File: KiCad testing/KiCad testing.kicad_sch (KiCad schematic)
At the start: 41 parts, among them J1 USB_A, Q1 IRF540N, Q2 IRF540N, Q3 IRF540N, U1 IR2113S, U2 IR2113S, U3 ACS712xLCTR-05B

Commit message: Update Schematic
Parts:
- removed U1, U2: IR2113S, Package_DIP:DIP-14_W7.62mm_Socket, symbol Driver_FET:IR2113S
- added U1, U4: IR2213, Package_DIP:DIP-14_W7.62mm, symbol Driver_FET:IR2213
- C1: renamed from C6; footprint (none) -> Capacitor_THT:CP_Radial_D5.0mm_P2.00mm
- C2: renamed from C9; footprint (none) -> Capacitor_THT:CP_Radial_D5.0mm_P2.00mm
- C3: footprint (none) -> Capacitor_THT:CP_Radial_D6.3mm_P2.50mm
- C4, C8: footprint (none) -> Capacitor_THT:C_Disc_D4.7mm_W2.5mm_P5.00mm
- C5: renamed from C7; footprint (none) -> Capacitor_THT:CP_Radial_D5.0mm_P2.00mm
- C6: renamed from C10; footprint (none) -> Capacitor_THT:CP_Radial_D5.0mm_P2.00mm
- C7: renamed from C11; footprint (none) -> Capacitor_THT:CP_Radial_D6.3mm_P2.50mm
- renumbered C12 to C10, C1 to C11, C5 to C12, C2 to C9, D2 to D1, D3 to D2, D5 to D3, D1 to D5, R5 to R2, R2 to R4, R6 to R5, R4 to R6, R9 to Rb1, R11 to Rb2
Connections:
- net +Buck_Boost_Load: now also U1.11 (SD), U1.13 (VSS), U1.2 (COM), U4.11 (SD), U4.13 (VSS), U4.2 (COM)
- net 12V: now also U1.3 (VCC), U4.3 (VCC)
- net 5V: now also U1.9 (VDD), U4.9 (VDD)
- net PWM_High: now also U4.10 (HIN)
- net PWM_Low: now also U4.12 (LIN)
- net PWM_MPPT: now also U1.10 (HIN)
- net VS: now also U4.5 (VS); no longer C6.2, R5.1
- net at R1.2: now also U4.1 (LO)
- net at C2.1, C3.1, C4.2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: now also U4.6 (VB)
- net at R3.1: now also U4.7 (HO)
- net at R4.2: now also U1.1 (LO)
- net at C6.1, C7.1, C8.2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: now also U1.6 (VB)
- net at R6.1: now also U1.7 (HO)
- new net VS_1: C6.2, R5.1, U1.5 (VS)

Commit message: Update Schematic
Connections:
- net PWM_High: now also A1.13 (D10); no longer A1.12 (D9)
- net PWM_Low: now also A1.12 (D9); no longer A1.13 (D10)

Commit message: Update Schematic
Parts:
- C2, C6: value 10uF -> 470uF; footprint Capacitor_THT:CP_Radial_D5.0mm_P2.00mm -> Capacitor_THT:CP_Radial_D10.0mm_P5.00mm
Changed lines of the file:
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@@
       (effects (font (size 1.27 1.27)) (justify right))
     )
-    (property "Value" "10uF" (at 114.173 93.599 0)
+    (property "Value" "470uF" (at 114.173 93.599 0)
       (effects (font (size 1.27 1.27)) (justify right))
     )
-    (property "Footprint" "Capacitor_THT:CP_Radial_D5.0mm_P2.00mm" (at 113.03 96.52 0)
+    (property "Footprint" "Capacitor_THT:CP_Radial_D10.0mm_P5.00mm" (at 113.03 96.52 0)
       (effects (font (size 1.27 1.27)) hide)
     )
@@
       (effects (font (size 1.27 1.27)) (justify right))
     )
-    (property "Value" "10uF" (at 114.173 38.989 0)
+    (property "Value" "470uF" (at 114.173 38.989 0)
       (effects (font (size 1.27 1.27)) (justify right))
     )
-    (property "Footprint" "Capacitor_THT:CP_Radial_D5.0mm_P2.00mm" (at 113.03 41.91 0)
-      (effects (font (size 1.27 1.27)) hide)
-    )
+    (property "Footprint" "Capacitor_THT:CP_Radial_D10.0mm_P5.00mm" (at 113.03 41.91 0)
+      (effects (font (size 1.27 1.27)) hide)
+    )

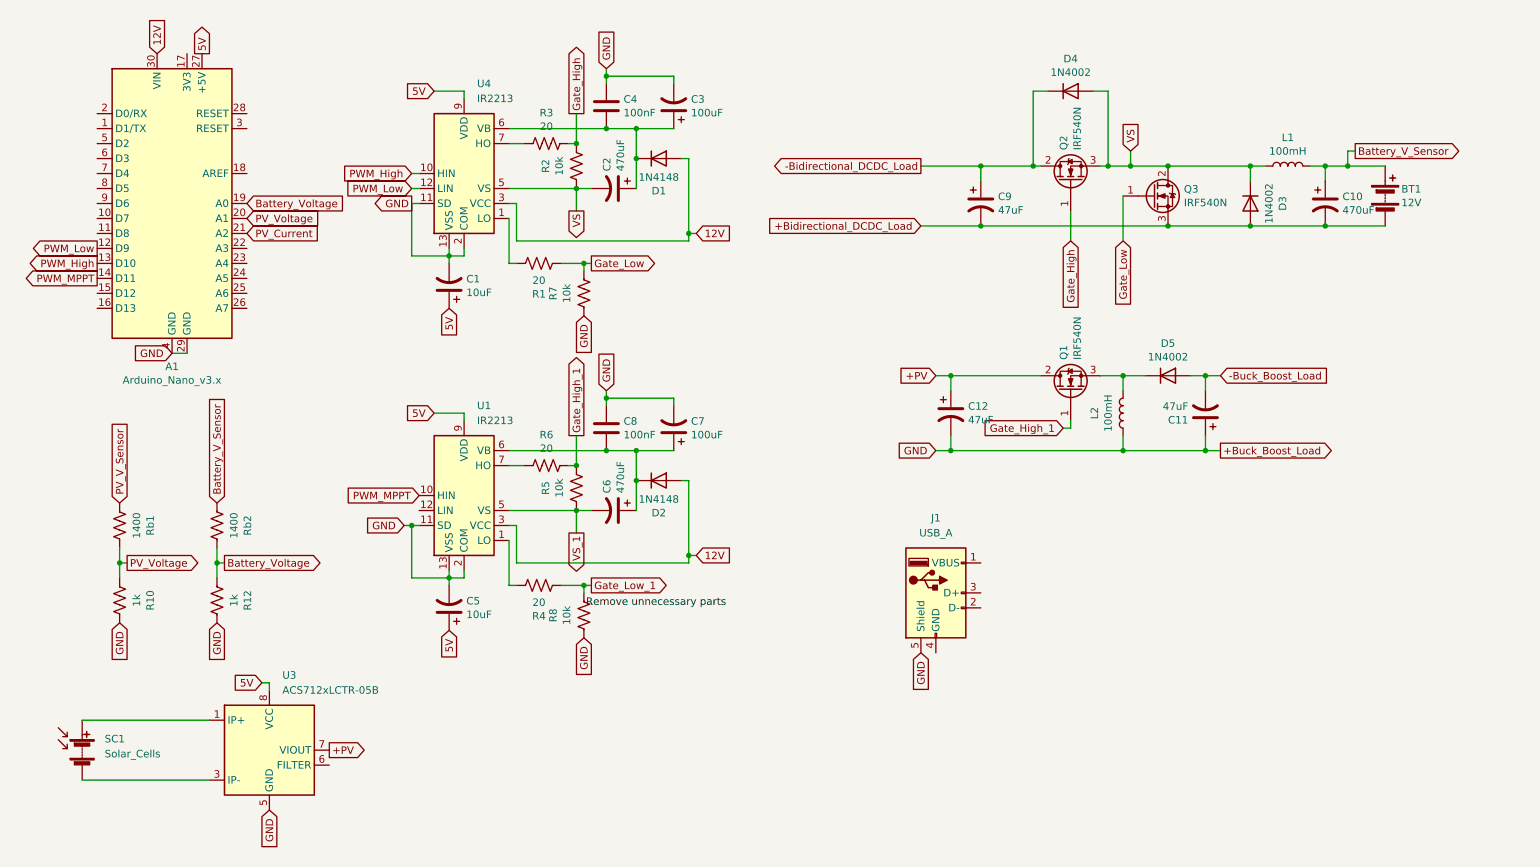
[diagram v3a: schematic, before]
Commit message: Update schematic and redesign pcb layout.
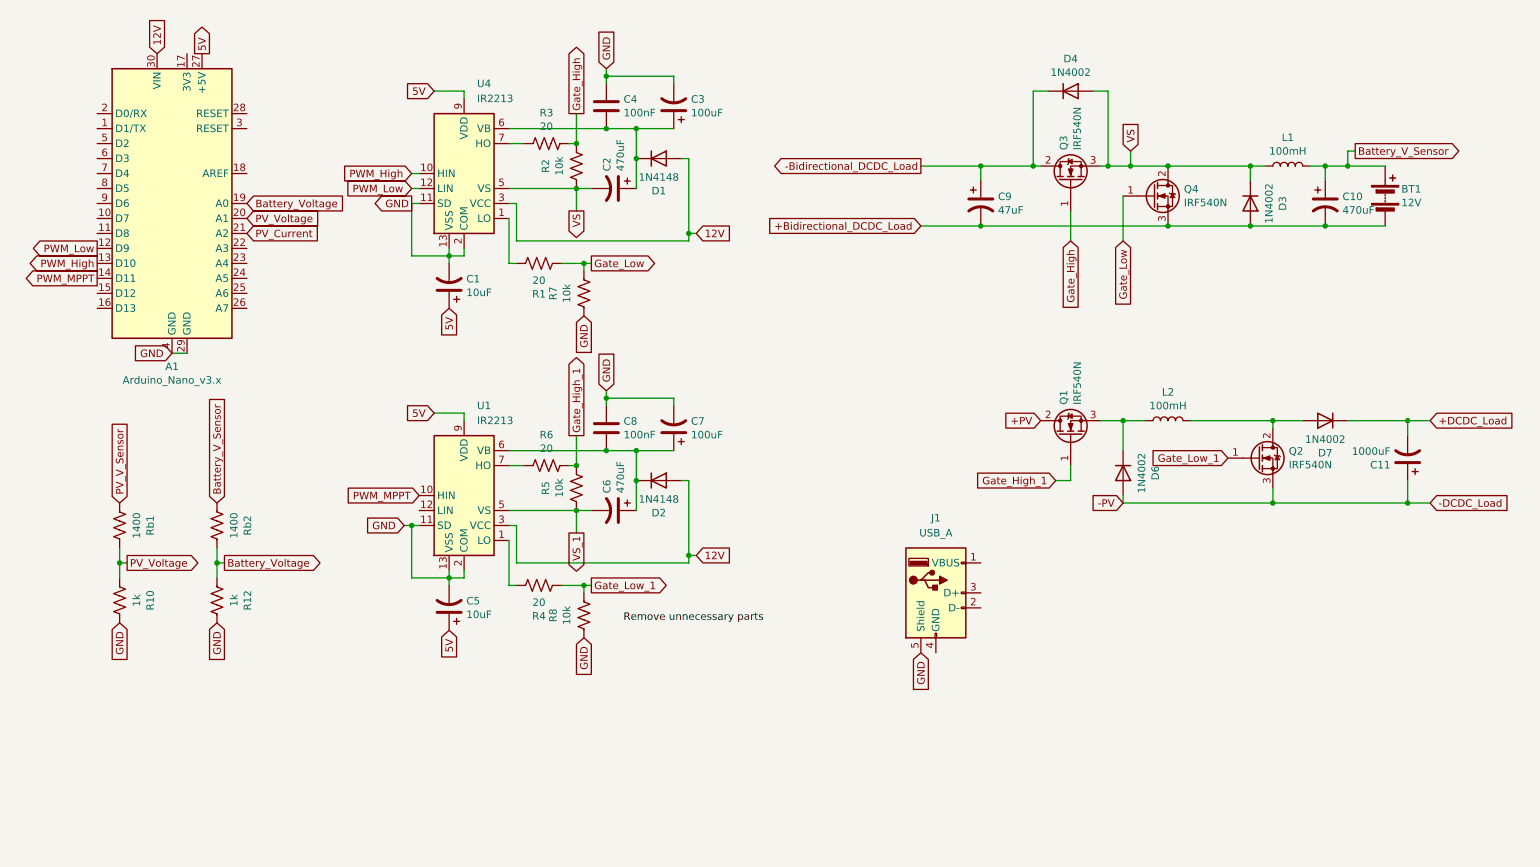
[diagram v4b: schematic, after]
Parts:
- removed C12: 47uF, Capacitor_THT:CP_Radial_D6.3mm_P2.50mm, symbol KiCad testing-rescue:CP1-Device
- removed D5: 1N4002, Diode_THT:D_DO-41_SOD81_P10.16mm_Horizontal, symbol Diode:1N4002
- removed SC1: Solar_Cells, symbol Device:Solar_Cells
- removed U3: ACS712xLCTR-05B, Package_SO:SOIC-8_3.9x4.9mm_P1.27mm, symbol Sensor_Current:ACS712xLCTR-05B
- added D6, D7: 1N4002, Diode_THT:D_DO-41_SOD81_P10.16mm_Horizontal, symbol Diode:1N4002
- added Q2: IRF540N, Package_TO_SOT_THT:TO-220-3_Vertical, symbol Transistor_FET:IRF540N
- C11: value 47uF -> 1000uF; footprint Capacitor_THT:CP_Radial_D6.3mm_P2.50mm -> Capacitor_THT:CP_Radial_D10.0mm_P5.00mm
- C3, C7: footprint Capacitor_THT:CP_Radial_D6.3mm_P2.50mm -> Capacitor_THT:CP_Radial_D5.0mm_P2.00mm
- renumbered Q2 to Q3, Q3 to Q4
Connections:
- net Gate_Low_1: now also Q2.1 (G)
- net at Q1.3 (S): now also L2.1, D6.1 (K); no longer L2.2
- net +Buck_Boost_Load renamed GND
- net GND: no longer C11.1, L2.1
- net -Buck_Boost_Load renamed +DCDC_Load
- net +DCDC_Load: now also D7.1 (K)
- new net: D7.2 (A), L2.2, Q2.2 (D)
- new net -DCDC_Load: C11.1, D6.2 (A), Q2.3 (S)

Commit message: update pcb
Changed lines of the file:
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@@
     )
   )
-  (global_label "+DCDC_Load" (shape input) (at 251.46 81.28 0) (fields_autoplaced)
+  (global_label "+DCDC_Load" (shape output) (at 251.46 81.28 0) (fields_autoplaced)
     (effects (font (size 1.27 1.27)) (justify left))
     (property "Intersheetrefs" "${INTERSHEET_REFS}" (at 265.8861 81.28 0)
